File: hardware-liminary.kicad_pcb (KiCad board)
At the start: 2 copper layers, 174.8 x 84.4 mm, 51 parts, among them IC1 MCP6001T-I_OT, J1 Conn_01x05, J2 Conn_01x05, J3 UFL-Conn, J4 SWD, J5 Console, J6 Nema 7-Pin, K1 HL2-1CH-12S, Q1 CMBT2222A, Q2 PT204-6C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

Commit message: Agregado modulo HLW8032
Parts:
- removed J1, J2: Conn_01x05, Connector_PinHeader_2.54mm:PinHeader_1x05_P2.54mm_Vertical
- added JB1: Conn_01x03, Connector_PinHeader_2.54mm:PinHeader_1x03_P2.54mm_Vertical, F.Cu at (55.5, 46.5)
- added JB2: Conn_01x03, Connector_PinHeader_2.54mm:PinHeader_1x03_P2.54mm_Vertical, F.Cu at (55.5, 52.5)
- added JB3: Conn_01x05, Connector_PinHeader_2.54mm:PinHeader_1x05_P2.54mm_Vertical, F.Cu at (55.5, 59.2)
- added JP5: Jumper_2_Open, Jumper:SolderJumper-2_P1.3mm_Open_TrianglePad1.0x1.5mm, F.Cu at (53.2, 118.1)
- added JT1: Conn_01x03, Connector_PinHeader_2.54mm:PinHeader_1x03_P2.54mm_Vertical, F.Cu at (69.8, 46.5)
- added JT2: Conn_01x03, Connector_PinHeader_2.54mm:PinHeader_1x03_P2.54mm_Vertical, F.Cu at (69.8, 52.5)
- added JT3: Conn_01x05, Connector_PinHeader_2.54mm:PinHeader_1x05_P2.54mm_Vertical, F.Cu at (69.8, 59.2)
- added R12: 10K, Resistor_SMD:R_1206_3216Metric_Pad1.42x1.75mm_HandSolder, F.Cu at (93.0, 125.6)
- added R13: 10K, Resistor_SMD:R_1206_3216Metric_Pad1.42x1.75mm_HandSolder, F.Cu at (82.5, 127.9)
- added R14: 20K, Resistor_SMD:R_1206_3216Metric_Pad1.42x1.75mm_HandSolder, F.Cu at (93.0, 131.6)
- added R15: 20K, Resistor_SMD:R_1206_3216Metric_Pad1.42x1.75mm_HandSolder, F.Cu at (82.5, 133.9)
- added U3: HLW8032_module, proyect_new:HLW8032_module, F.Cu at (73.5, 119.6)
- moved BAT1 291.6 mm to (117.8, 280.3)
- moved AE1 274.9 mm to (129.8, 209.8)
- moved C1 274.9 mm to (37.5, 218.8)
- moved C10 274.9 mm to (39.8, 294.6)
- moved C2 274.9 mm to (22.5, 221.8)
- moved C3 274.9 mm to (73.5, 228.6)
- moved C4 274.9 mm to (81.0, 228.6)
- moved C5 274.9 mm to (56.2, 238.3)
- moved C6 274.9 mm to (30.8, 251.8)
- moved C7 274.9 mm to (54.8, 253.3)
- moved C8 274.9 mm to (60.8, 253.3)
- moved C9 274.9 mm to (69.0, 266.8)
- moved IC1 274.9 mm to (60.0, 222.6)
- moved J3 274.9 mm to (131.2, 219.6)
- moved J4 274.9 mm to (114.8, 257.1)
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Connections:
- U1 pad 19: (no net) -> /Top Board/Relay
- U1 pad 21: /Top Board/Relay -> /Top Board/Enery_Pulses
- U1 pad 23: (no net) -> /Top Board/Enery_Tx

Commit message: Esquematico reordenado
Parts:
- moved JT2 264.6 mm to (11.8, 310.6), turned to 180 degrees
- moved JT3 263.4 mm to (48.6, 321.8), turned to 90 degrees
- moved JT1 202.6 mm to (134.5, 238.5)
- moved D1 195.3 mm to (210.5, 36.5)
- moved JP4 195.3 mm to (225.5, 20.8)
- moved JP5 195.3 mm to (225.5, 26.1)
- moved Q3 195.3 mm to (217.2, 41.0)
- moved R11 195.3 mm to (224.0, 41.0)
- moved K1 163.3 mm to (177.4, 35.7)
- moved JB2 150.0 mm to (205.2, 60.8)
- moved J6 131.5 mm to (148.7, 50.9)
- moved PS1 94.6 mm to (133.6, 79.6), turned to 90 degrees
- moved U3 90.0 mm to (77.3, 29.7)
- moved RV1 73.9 mm to (99.1, 88.5), turned to 270 degrees
- moved Q2 59.8 mm to (96.7, 217.3), turned to 180 degrees
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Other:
- board outline removed
- net class Load added: clearance 0.4, trace_width 1, via_dia 1.2, via_drill 0.4

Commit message: completado pcb
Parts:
- removed JP5: Jumper_2_Open, Jumper:SolderJumper-2_P1.3mm_Open_TrianglePad1.0x1.5mm
- removed R12, R13: 10K, Resistor_SMD:R_1206_3216Metric_Pad1.42x1.75mm_HandSolder
- removed R14, R15: 20K, Resistor_SMD:R_1206_3216Metric_Pad1.42x1.75mm_HandSolder
- removed U3: HLW8032_module, proyect_new:HLW8032_module
- JP4, JT1, JT2, JT3: moved to B.Cu
- moved JT2 300.3 mm to (218.2, 92.5)
- moved JT3 291.0 mm to (179.1, 61.7), turned to 270 degrees
- moved C10 260.3 mm to (191.7, 92.2), turned to 180 degrees
- moved U1 231.9 mm to (198.6, 114.0), turned to 180 degrees
- moved R9 227.8 mm to (177.5, 103.9)
- moved C6 222.2 mm to (199.6, 118.9), turned to 180 degrees
- moved R10 221.8 mm to (177.5, 100.1), turned to 180 degrees
- moved LED1 218.8 mm to (169.7, 103.1), turned to 180 degrees
- moved J5 199.0 mm to (187.2, 125.0), turned to 270 degrees
- moved BAT1 196.4 mm to (195.3, 125.0), turned to 270 degrees
- moved R6 193.9 mm to (160.0, 85.3), turned to 180 degrees
- moved Q1 193.1 mm to (154.5, 86.8), turned to 270 degrees
- moved C7 192.8 mm to (173.0, 110.3), turned to 270 degrees
- moved C9 191.3 mm to (165.6, 110.0), turned to 270 degrees
- moved C8 190.0 mm to (178.8, 113.8), turned to 270 degrees
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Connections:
- J4 pad 6: (no net) -> Net-(J4-Pad6)
- J4 pad 7: (no net) -> Net-(J4-Pad7)
- J4 pad 8: (no net) -> Net-(J4-Pad8)
- JB1 pad 2: (no net) -> Net-(JB1-Pad2)
- JB2 pad 2: (no net) -> Net-(JB2-Pad2)
- JB3 pad 2: (no net) -> Net-(JB3-Pad2)
- JB3 pad 4: (no net) -> Net-(JB3-Pad4)
- JT1 pad 2: (no net) -> Net-(JT1-Pad2)
- JT2 pad 2: (no net) -> Net-(JT2-Pad2)
- JT3 pad 2: (no net) -> Net-(JT3-Pad2)
- JT3 pad 4: (no net) -> Net-(JT3-Pad4)
- K1 pad 2: (no net) -> Net-(K1-Pad2)
- U1 pad 11: (no net) -> Net-(U1-Pad11)
- U1 pad 14: (no net) -> Net-(U1-Pad14)
- U1 pad 15: (no net) -> Net-(U1-Pad15)
- U1 pad 17: (no net) -> Net-(U1-Pad17)
- U1 pad 22: (no net) -> Net-(U1-Pad22)
- U1 pad 27: (no net) -> Net-(U1-Pad27)
- U1 pad 28: (no net) -> Net-(U1-Pad28)
- U1 pad 29: (no net) -> Net-(U1-Pad29)
- U1 pad 30: (no net) -> Net-(U1-Pad30)
- U1 pad 36: (no net) -> Net-(U1-Pad36)
- U1 pad 39: (no net) -> Net-(U1-Pad39)
- U1 pad 41: (no net) -> Net-(U1-Pad41)
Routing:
- net GNDD: track 0.00 -> 253.6 mm, vias 0 -> 3
- net /Top Board/3.3v: track 0.00 -> 196.1 mm, vias 0 -> 3
- net /Bottom Board/+12v: track 0.00 -> 84.0 mm, vias 0 -> 1
- net GNDREF: track 0.00 -> 74.4 mm, vias 0 -> 1
- net /Bottom Board/Linea: track 0.00 -> 62.3 mm
- net /Top Board/Reset: track 0.00 -> 59.6 mm, vias 0 -> 1
- net Net-(C14-Pad1): track 0.00 -> 47.8 mm
- net /Top Board/Enery_Tx: track 0.00 -> 43.3 mm, vias 0 -> 1
- net /Top Board/Relay: track 0.00 -> 43.1 mm, vias 0 -> 1
- net /Bottom Board/Neutro: track 0.00 -> 40.9 mm
- net /Top Board/Enery_Pulses: track 0.00 -> 40.7 mm, vias 0 -> 1
- net GNDA: track 0.00 -> 33.0 mm, vias 0 -> 1
- net /Top Board/SWDIO: track 0.00 -> 27.4 mm, vias 0 -> 1
- net /Top Board/PIR: track 0.00 -> 26.9 mm, vias 0 -> 1
- net /Bottom Board/Carga: track 0.00 -> 25.1 mm
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- added copper zone on B.Cu, net GNDA
- added copper zone on F.Cu, net GNDA
- added copper zone on B.Cu, net GNDD
- added copper zone on F.Cu, net GNDD
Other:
- board outline added: 149.2 x 73 mm
- net class Default: trace_width 0.25 -> 0.7
- net class Load: clearance 0.4 -> 1.5; trace_width 1 -> 1.5

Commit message: Correciones menores
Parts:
- moved PS1 0.57 mm to (123.4, 105.6)
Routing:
- net /Bottom Board/Linea: track 62.3 -> 60.8 mm
- net /Bottom Board/+12v: track 84.0 -> 83.5 mm
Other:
- net class Load: clearance 1.5 -> 1
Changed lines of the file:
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@@
     (thickness 1.6)
     (drawings 3)
-    (tracks 387)
+    (tracks 385)
     (zones 0)
     (modules 55)
@@
   )
   (net_class Load ""
-    (clearance 1.5)
+    (clearance 1)
     (trace_width 1.5)
     (via_dia 1.2)
@@
       (effects (font (size 1 1) (thickness 0.15)))
     )
-    (fp_circle (center 0 0) (end 36 0) (layer F.CrtYd) (width 0.12))
+    (fp_circle (center 0 0) (end 36 0) (layer Cmts.User) (width 0.12))
+    (pad 5 thru_hole circle (at -23 5.475) (size 1.5 1.5) (drill 0.8) (layers *.Cu *.Mask)
+      (net 15 GNDREF))
+    (pad 4 thru_hole circle (at -23 -5.525) (size 1.5 1.5) (drill 0.8) (layers *.Cu *.Mask)
+      (net 20 "/Bottom Board/OpenC"))
+    (pad 2 thru_hole circle (at -7 5.775) (size 3.2 3.2) (drill 2.25) (layers *.Cu *.Mask)
+      (net 31 "/Bottom Board/Neutro"))
+    (pad 1 thru_hole circle (at 0 -7.525) (size 3.2 3.2) (drill 2.25) (layers *.Cu *.Mask)
+      (net 30 "/Bottom Board/Linea"))
+    (pad 3 thru_hole circle (at 8.5 3.875) (size 3.2 3.2) (drill 2.25) (layers *.Cu *.Mask)
+      (net 29 "/Bottom Board/Carga"))
+    (pad 6 thru_hole circle (at 23 -3.525) (size 1.5 1.5) (drill 0.8) (layers *.Cu *.Mask)
+      (net 18 "/Bottom Board/3.3v"))
     (pad 7 thru_hole circle (at 23 7.475) (size 1.5 1.5) (drill 0.8) (layers *.Cu *.Mask)
       (net 19 "/Bottom Board/PIR"))
-    (pad 6 thru_hole circle (at 23 -3.525) (size 1.5 1.5) (drill 0.8) (layers *.Cu *.Mask)
-      (net 18 "/Bottom Board/3.3v"))
-    (pad 3 thru_hole circle (at 8.5 3.875) (size 3.2 3.2) (drill 2.25) (layers *.Cu *.Mask)
-      (net 29 "/Bottom Board/Carga"))
-    (pad 1 thru_hole circle (at 0 -7.525) (size 3.2 3.2) (drill 2.25) (layers *.Cu *.Mask)
-      (net 30 "/Bottom Board/Linea"))
-    (pad 2 thru_hole circle (at -7 5.775) (size 3.2 3.2) (drill 2.25) (layers *.Cu *.Mask)
-      (net 31 "/Bottom Board/Neutro"))
-    (pad 4 thru_hole circle (at -23 -5.525) (size 1.5 1.5) (drill 0.8) (layers *.Cu *.Mask)
-      (net 20 "/Bottom Board/OpenC"))
-    (pad 5 thru_hole circle (at -23 5.475) (size 1.5 1.5) (drill 0.8) (layers *.Cu *.Mask)
-      (net 15 GNDREF))
   )
   (module Resistor_SMD:R_1206_3216Metric_Pad1.42x1.75mm_HandSolder (layer F.Cu)
@@
   )
   (module proyect_new:Converter_ACDC_MeanWell_IRM-03-xx_THT (layer F.Cu)
-    (at 123.444 106.172 270)
+    (at 123.444 105.6005 270)
     (descr "ACDC-Converter, 3W, Meanwell, IRM-03, THT, https://www.meanwell.com/Upload/PDF/IRM-03/IRM-03-SPEC.PDF")
     (tags "ACDC-Converter 3W THT")
@@
   (segment (start 100.584 82.804) (end 102.108 81.28) (width 0.7) (layer B.Cu) (net 12))
   (segment (start 95.504 82.804) (end 100.584 82.804) (width 0.7) (layer B.Cu) (net 12))
-  (segment (start 88.138 116.332) (end 96.012 116.332) (width 0.7) (layer B.Cu) (net 12))
-  (segment (start 98.044 118.364) (end 96.012 116.332) (width 0.7) (layer B.Cu) (net 12))
-  (segment (start 98.044 123.952) (end 98.044 118.364) (width 0.7) (layer B.Cu) (net 12))
   (segment (start 95.504 92.456) (end 95.504 82.804) (width 0.7) (layer B.Cu) (net 12))
   (segment (start 95.504 96.266) (end 95.504 92.456) (width 0.7) (layer B.Cu) (net 12))
   (segment (start 88.138 112.522) (end 88.138 103.632) (width 0.7) (layer B.Cu) (net 12))
   (segment (start 88.138 103.632) (end 95.504 96.266) (width 0.7) (layer B.Cu) (net 12))
-  (segment (start 83.852 117.46337) (end 83.852 116.332) (width 0.7) (layer B.Cu) (net 13))
-  (segment (start 90.34063 123.952) (end 83.852 117.46337) (width 0.7) (layer B.Cu) (net 13))
-  (segment (start 92.964 123.952) (end 90.34063 123.952) (width 0.7) (layer B.Cu) (net 13))
+  (segment (start 98.044 123.3805) (end 98.044 118.364) (width 0.7) (layer B.Cu) (net 12))
+  (segment (start 96.012 116.332) (end 88.138 116.332) (width 0.7) (layer B.Cu) (net 12))
+  (segment (start 98.044 118.364) (end 96.012 116.332) (width 0.7) (layer B.Cu) (net 12))
   (via (at 80.772 112.522) (size 0.8) (drill 0.4) (layers F.Cu B.Cu) (net 13))
   (segment (start 80.772 111.462) (end 82.76 109.474) (width 0.7) (layer F.Cu) (net 13))
@@
   (segment (start 82.804 104.14) (end 82.76 104.184) (width 0.7) (layer F.Cu) (net 13))
   (segment (start 78.994 104.14) (end 82.804 104.14) (width 0.7) (layer F.Cu) (net 13))
+  (segment (start 83.852 117.46337) (end 83.852 116.332) (width 0.7) (layer B.Cu) (net 13))
+  (segment (start 92.964 123.3805) (end 89.76913 123.3805) (width 0.7) (layer B.Cu) (net 13))
+  (segment (start 89.76913 123.3805) (end 83.852 117.46337) (width 0.7) (layer B.Cu) (net 13))
   (segment (start 89.662 84.052) (end 89.176 83.566) (width 0.7) (layer F.Cu) (net 14))
   (segment (start 89.662 90.424) (end 89.662 84.052) (width 0.7) (layer F.Cu) (net 14))
@@
   (segment (start 131.064 87.376) (end 133.604 84.836) (width 1.5) (layer B.Cu) (net 29))
   (segment (start 128.1929 87.376) (end 131.064 87.376) (width 1.5) (layer B.Cu) (net 29))
-  (segment (start 123.19 106.2736) (end 123.19 106.1236) (width 1.5) (layer B.Cu) (net 30))
-  (segment (start 126.358 109.086) (end 123.444 106.172) (width 1.5) (layer B.Cu) (net 30))
-  (segment (start 131.194 109.086) (end 126.358 109.086) (width 1.5) (layer B.Cu) (net 30))
-  (segment (start 108.1913 89.740341) (end 108.1913 87.4776) (width 1.5) (layer B.Cu) (net 30))
-  (segment (start 110.49 102.87) (end 108.1913 100.5713) (width 1.5) (layer B.Cu) (net 30))
-  (segment (start 108.1913 100.5713) (end 108.1913 89.740341) (width 1.5) (layer B.Cu) (net 30))
-  (segment (start 123.444 106.172) (end 123.444 103.886) (width 1.5) (layer B.Cu) (net 30))
-  (segment (start 123.444 103.886) (end 122.428 102.87) (width 1.5) (layer B.Cu) (net 30))
-  (segment (start 122.428 102.87) (end 110.49 102.87) (width 1.5) (layer B.Cu) (net 30))
   (segment (start 121.3104 87.4776) (end 108.1913 87.4776) (width 1.5) (layer B.Cu) (net 30))
   (segment (start 125.7808 81.28) (end 125.7808 83.0072) (width 1.5) (layer B.Cu) (net 30))
   (segment (start 125.7808 83.0072) (end 121.3104 87.4776) (width 1.5) (layer B.Cu) (net 30))
-  (segment (start 116.737655 106.172) (end 118.364 106.172) (width 1.5) (layer B.Cu) (net 31))
-  (segment (start 101.1913 103.040341) (end 104.322959 106.172) (width 1.5) (layer B.Cu) (net 31))
-  (segment (start 104.322959 106.172) (end 116.737655 106.172) (width 1.5) (layer B.Cu) (net 31))
+  (segment (start 126.9295 109.086) (end 123.444 105.6005) (width 1.5) (layer B.Cu) (net 30))
+  (segment (start 131.194 109.086) (end 126.9295 109.086) (width 1.5) (layer B.Cu) (net 30))
+  (segment (start 123.444 103.632) (end 122.174 102.362) (width 1.5) (layer B.Cu) (net 30))
+  (segment (start 112.014 102.362) (end 108.1913 98.5393) (width 1.5) (layer B.Cu) (net 30))
+  (segment (start 123.444 105.6005) (end 123.444 103.632) (width 1.5) (layer B.Cu) (net 30))
+  (segment (start 108.1913 89.740341) (end 108.1913 87.4776) (width 1.5) (layer B.Cu) (net 30))
+  (segment (start 122.174 102.362) (end 112.014 102.362) (width 1.5) (layer B.Cu) (net 30))
+  (segment (start 108.1913 98.5393) (end 108.1913 89.740341) (width 1.5) (layer B.Cu) (net 30))
+  (segment (start 121.158 116.586) (end 129.794 116.586) (width 1.5) (layer B.Cu) (net 31))
+  (segment (start 101.1913 103.040341) (end 104.020969 105.87001) (width 1.5) (layer B.Cu) (net 31))
+  (segment (start 118.364 105.87001) (end 118.364 113.792) (width 1.5) (layer B.Cu) (net 31))
   (segment (start 101.1913 100.7776) (end 101.1913 103.040341) (width 1.5) (layer B.Cu) (net 31))
-  (segment (start 118.364 113.792) (end 118.364 106.172) (width 1.5) (layer B.Cu) (net 31))
-  (segment (start 129.794 116.586) (end 121.158 116.586) (width 1.5) (layer B.Cu) (net 31))
-  (segment (start 121.158 116.586) (end 118.364 113.792) (width 1.5) (layer B.Cu) (net 31))
+  (segment (start 104.020969 105.87001) (end 118.364 105.87001) (width 1.5) (layer B.Cu) (net 31))
+  (segment (start 118.364 113.792) (end 121.158 116.586) (width 1.5) (layer B.Cu) (net 31))
   (segment (start 207.005 109.596) (end 207.01 109.601) (width 0.7) (layer F.Cu) (net 32))
   (segment (start 200.878 109.596) (end 207.005 109.596) (width 1) (layer F.Cu) (net 32))

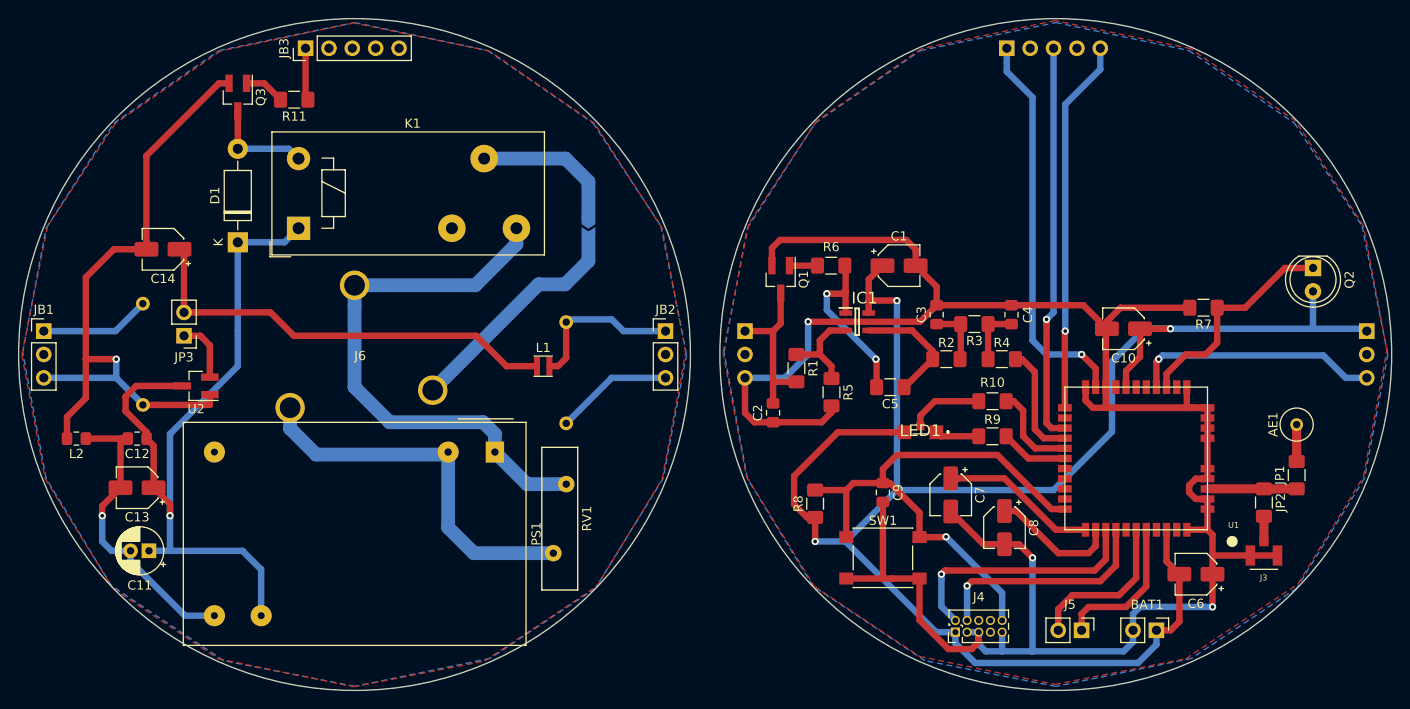
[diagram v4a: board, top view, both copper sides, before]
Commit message: conector nema rotado y reordenada la placa superior
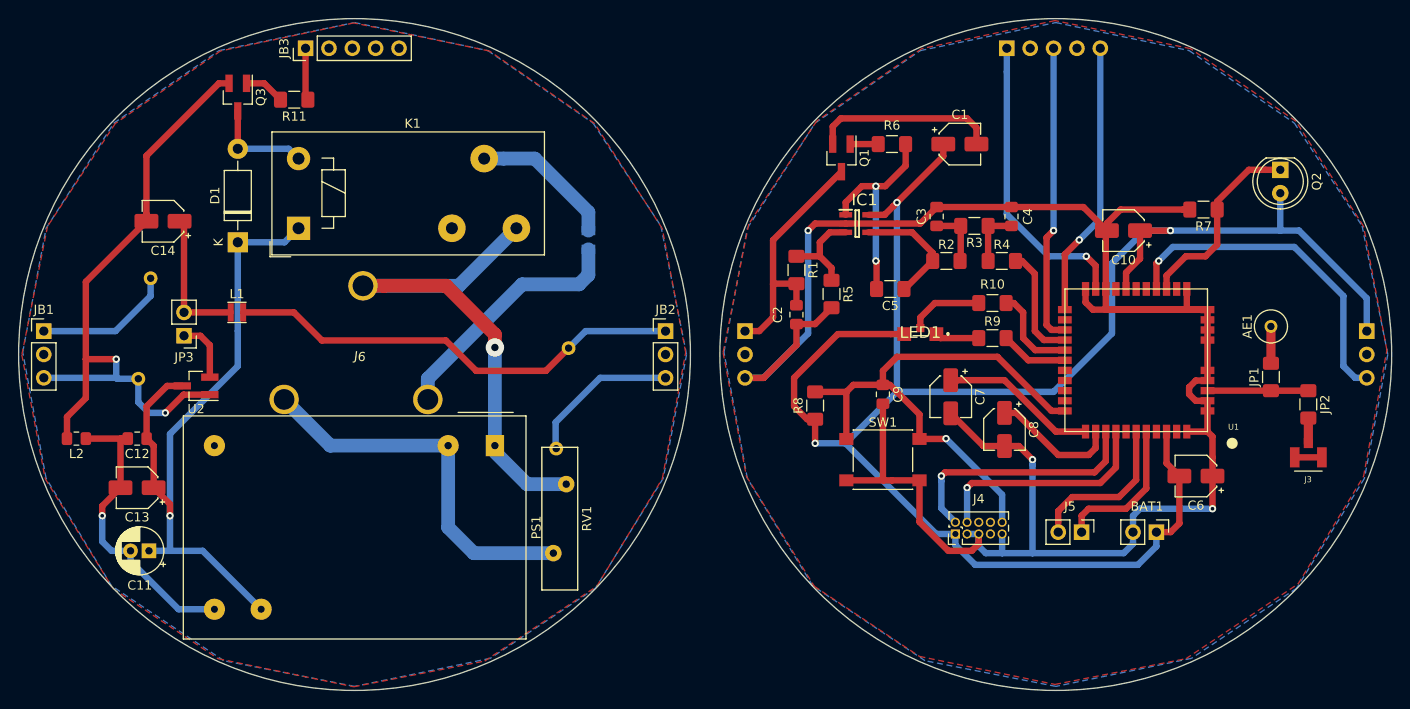
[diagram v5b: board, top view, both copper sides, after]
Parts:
- JP4: footprint Jumper:SolderJumper-2_P1.3mm_Open_TrianglePad1.0x1.5mm -> Jumper:SolderJumper-2_P1.3mm_Open_Pad1.0x1.5mm
- moved L1 33.8 mm to (95.4, 90.4)
- moved Q1 14.8 mm to (161.1, 73.6)
- moved R6 14.8 mm to (166.6, 72.1)
- moved C1 14.8 mm to (174.0, 72.1)
- moved J3 11.7 mm to (211.8, 106.2)
- moved JP2 11.7 mm to (211.8, 100.4)
- moved Q2 11.2 mm to (208.8, 74.9)
- moved AE1 11.0 mm to (207.8, 91.9)
- moved JP1 11.0 mm to (207.8, 97.4)
- moved C2 11.0 mm to (156.2, 90.7)
- moved BAT1 10.7 mm to (195.3, 114.3)
- moved C5 10.7 mm to (166.4, 87.9)
- moved C6 10.7 mm to (199.6, 108.2)
- moved C9 10.7 mm to (165.6, 99.3)
- moved J4 10.7 mm to (173.5, 114.5)
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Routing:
- net /Bottom Board/3.3v: track 17.5 -> 50.3 mm
- net Net-(C14-Pad1): track 47.8 -> 15.2 mm
- net /Top Board/Enery_Pulses: track 40.7 -> 30.0 mm
- net /Top Board/Enery_Tx: track 43.3 -> 32.6 mm
- net /Top Board/Relay: track 43.1 -> 32.5 mm
- net /Top Board/3.3v: track 196.1 -> 206.2 mm
- net /Top Board/PIR: track 26.9 -> 36.7 mm
- net /Top Board/OpenC: track 17.9 -> 27.5 mm
- net /Bottom Board/+12v: track 83.5 -> 76.4 mm
- net /Bottom Board/PIR: track 12.8 -> 16.8 mm
- net /Bottom Board/Linea: track 60.8 -> 57.1 mm, vias 0 -> 1
- net Net-(C5-Pad2): track 19.7 -> 23.1 mm
- net /Bottom Board/OpenC: track 12.0 -> 15.1 mm
- net /Top Board/Photocell: track 24.4 -> 21.3 mm
- net /Bottom Board/Carga: track 25.1 -> 27.2 mm
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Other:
- net class Load: clearance 1 -> 0.2; via_dia 1.2 -> 2; via_drill 0.4 -> 0.8
